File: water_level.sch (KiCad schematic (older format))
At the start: 14 parts, among them U1 LTV-847

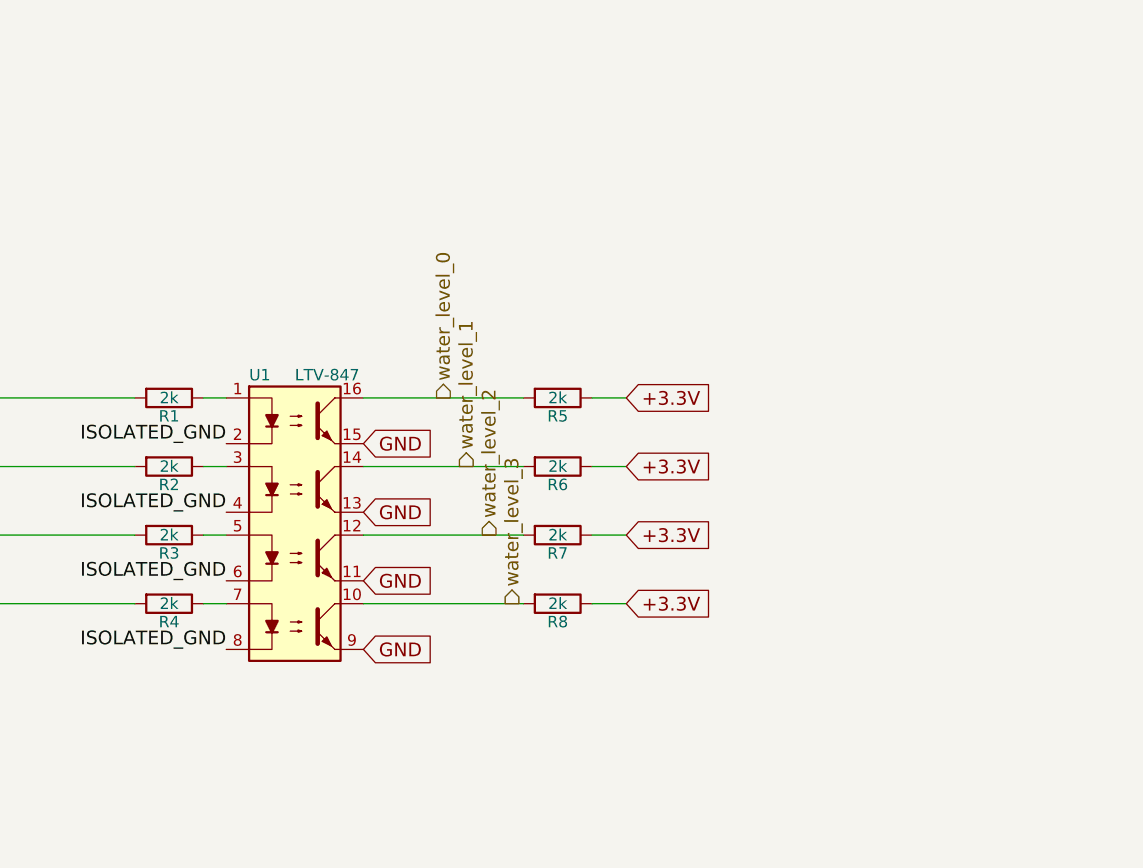
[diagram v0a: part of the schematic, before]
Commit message: fixed links to the webpage of parts
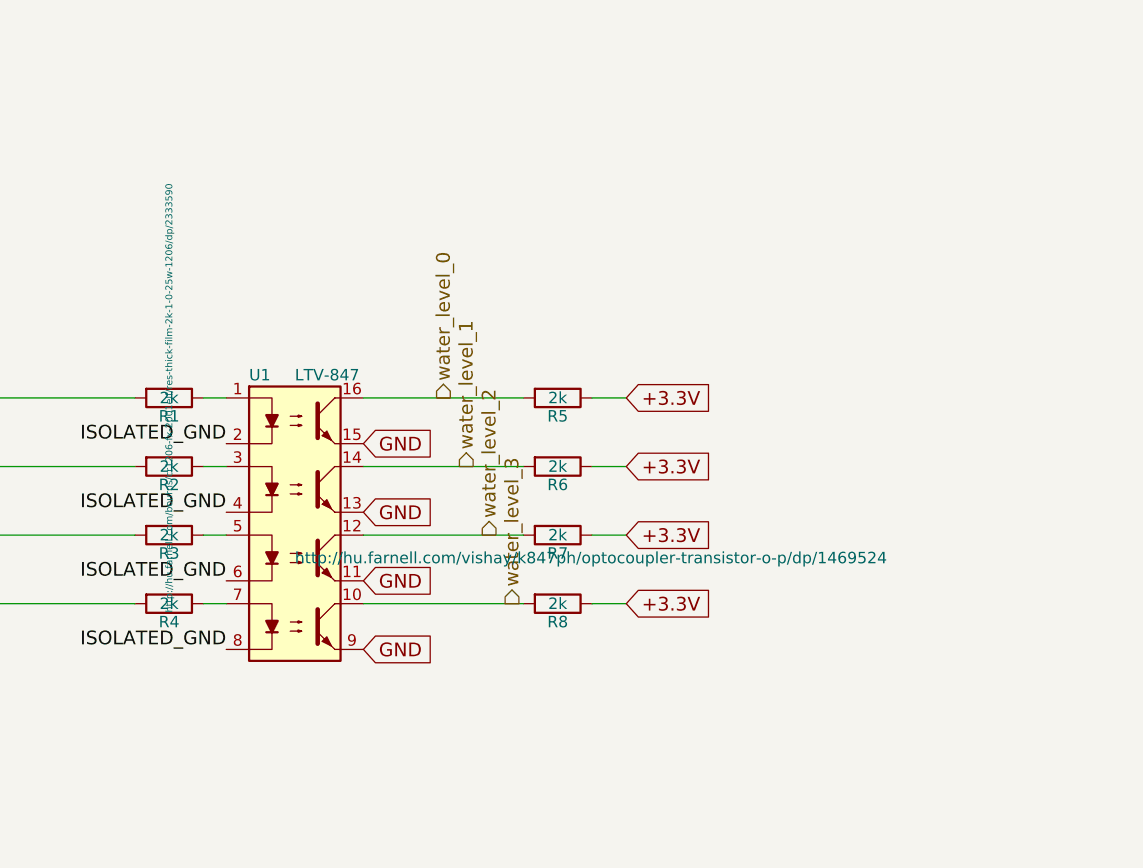
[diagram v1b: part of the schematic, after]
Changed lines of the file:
@@
 F 1 "LTV-847" H 7350 3850 50  0000 L CNN
 F 2 "Housings_SOIC:SOIC-16_3.9x9.9mm_Pitch1.27mm" H 7150 2550 50  0001 L CIN
-F 3 "" H 7350 3050 50  0000 L CNN
+F 3 "http://hu.farnell.com/vishay/k847ph/optocoupler-transistor-o-p/dp/1469524" H 7350 3050 50  0000 L CNN
 	1    7350 3150
 	1    0    0    -1
@@
 F 1 "2k" V 6800 2550 50  0000 C CNN
 F 2 "Resistors_SMD:R_1206_HandSoldering" V 6730 2550 30  0001 C CNN
-F 3 "" H 6800 2550 30  0000 C CNN
+F 3 "http://hu.farnell.com/bourns/cr1206-fx-2001elf/res-thick-film-2k-1-0-25w-1206/dp/2333590" H 6800 2550 30  0000 C CNN
 	1    6800 2550
 	0    1    1    0
@@
 F 1 "CME0303S3C" H 1500 950 60  0000 C CNN
 F 2 "water:CME0303S3C" H 1500 950 60  0001 C CNN
-F 3 "http://uk.farnell.com/murata-power-solutions/cme0303s3c/dc-dc-conv-iso-pol-1o-p-0-75w/dp/2400810" H 1500 950 60  0001 C CNN
+F 3 "http://hu.farnell.com/murata-power-solutions/cme0303s3c/dc-dc-conv-iso-pol-1o-p-0-75w/dp/2400810" H 1500 950 60  0001 C CNN
 	1    1500 950
 	1    0    0    -1

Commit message: updated links
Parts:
- DC-DC_ISOLATED1: value CME0303S3C -> MCE05S15D
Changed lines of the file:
@@
 P 1500 950
 F 0 "DC-DC_ISOLATED1" H 1550 200 60  0000 C CNN
-F 1 "CME0303S3C" H 1500 950 60  0000 C CNN
+F 1 "MCE05S15D" H 1500 950 60  0000 C CNN
 F 2 "water:CME0303S3C" H 1500 950 60  0001 C CNN
-F 3 "http://hu.farnell.com/murata-power-solutions/cme0303s3c/dc-dc-conv-iso-pol-1o-p-0-75w/dp/2400810" H 1500 950 60  0001 C CNN
+F 3 "http://hu.farnell.com/multicomp/mce05s15d/dc-dc-converter-1w-single-o-p/dp/2079693" H 1500 950 60  0001 C CNN
 	1    1500 950
 	1    0    0    -1

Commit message: stash commit before the revision of the parts
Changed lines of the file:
@@
 F 1 "LTV-847" H 7350 3850 50  0000 L CNN
 F 2 "Housings_SOIC:SOIC-16_3.9x9.9mm_Pitch1.27mm" H 7150 2550 50  0001 L CIN
-F 3 "http://hu.farnell.com/vishay/k847ph/optocoupler-transistor-o-p/dp/1469524" H 7350 3050 50  0000 L CNN
+F 3 "http://hu.farnell.com/vishay/k847ph/optocoupler-transistor-o-p/dp/1469524" H 7350 3050 50  0001 L CNN
 	1    7350 3150
 	1    0    0    -1
@@
 F 1 "2k" V 6800 2550 50  0000 C CNN
 F 2 "Resistors_SMD:R_1206_HandSoldering" V 6730 2550 30  0001 C CNN
-F 3 "http://hu.farnell.com/bourns/cr1206-fx-2001elf/res-thick-film-2k-1-0-25w-1206/dp/2333590" H 6800 2550 30  0000 C CNN
+F 3 "http://hu.farnell.com/bourns/cr1206-fx-2001elf/res-thick-film-2k-1-0-25w-1206/dp/2333590" H 6800 2550 30  0001 C CNN
 	1    6800 2550
 	0    1    1    0
@@
 +5V
 $Comp
+L Water_Level_Sensor_Connector SENS_1
+U 1 1 592601C6
+P 3600 2600
+F 0 "SENS_1" H 3450 1500 60  0000 C CNN
+F 1 "Water_Level_Sensor_Connector" H 3600 2600 60  0000 C CNN
+F 2 "Connectors_Terminal_Blocks:TerminalBlock_WAGO-804_RM5mm_5pol" H 3600 2600 60  0001 C CNN
+F 3 "http://hu.farnell.com/wago/2604-1105/tb-wire-to-brd-5pos-12awg/dp/2749668" H 3600 2600 60  0001 C CNN
+	1    3600 2600
+	1    0    0    -1
+$EndComp
+$Comp
+L Water_Level_Sensor_Connector SENS_3
+U 1 1 59260240
+P 3600 5150
+F 0 "SENS_3" H 3450 4050 60  0000 C CNN
+F 1 "Water_Level_Sensor_Connector" H 3600 5150 60  0000 C CNN
+F 2 "Connectors_Terminal_Blocks:TerminalBlock_WAGO-804_RM5mm_5pol" H 3600 5150 60  0001 C CNN
+F 3 "http://hu.farnell.com/wago/2604-1105/tb-wire-to-brd-5pos-12awg/dp/2749668" H 3600 5150 60  0001 C CNN
+	1    3600 5150
+	1    0    0    -1
+$EndComp
+$Comp
+L Water_Level_Sensor_Connector SENS_4
+U 1 1 592602C7
+P 3600 6400
+F 0 "SENS_4" H 3450 5300 60  0000 C CNN
+F 1 "Water_Level_Sensor_Connector" H 3600 6400 60  0000 C CNN
+F 2 "Connectors_Terminal_Blocks:TerminalBlock_WAGO-804_RM5mm_5pol" H 3600 6400 60  0001 C CNN
+F 3 "http://hu.farnell.com/wago/2604-1105/tb-wire-to-brd-5pos-12awg/dp/2749668" H 3600 6400 60  0001 C CNN
+	1    3600 6400
+	1    0    0    -1
+$EndComp
+Wire Wire Line
+	7650 2550 8350 2550
+Wire Wire Line
+	7650 2850 8350 2850
+Wire Wire Line
+	7650 3150 8350 3150
+Wire Wire Line
+	7650 3450 8350 3450
+Wire Wire Line
+	8800 2550 8650 2550
+Wire Wire Line
+	8800 2850 8650 2850
+Wire Wire Line
+	8800 3150 8650 3150
+Wire Wire Line
+	8800 3450 8650 3450
+Wire Wire Line
+	6950 3450 7050 3450
+Wire Wire Line
+	6950 3150 7050 3150
+Wire Wire Line
+	6950 2850 7050 2850
+Wire Wire Line
+	6950 2550 7050 2550
+Text GLabel 7650 3650 2    60   Input ~ 0
+GND
+Text GLabel 7650 3350 2    60   Input ~ 0
+GND
+Text GLabel 7650 3050 2    60   Input ~ 0
+GND
+Text GLabel 7650 2750 2    60   Input ~ 0
+GND
+Text GLabel 8800 2550 2    60   Input ~ 0
++3.3V
+Text GLabel 8800 2850 2    60   Input ~ 0
++3.3V
+Text GLabel 8800 3150 2    60   Input ~ 0
++3.3V
+Text GLabel 8800 3450 2    60   Input ~ 0
++3.3V
+Text Label 2000 1200 0    60   ~ 0
+ISOLATED_GND
+Text Label 3100 2850 2    60   ~ 0
+ISOLATED_GND
+Text Label 3100 4100 2    60   ~ 0
+ISOLATED_GND
+Text Label 3100 5400 2    60   ~ 0
+ISOLATED_GND
+Text Label 3100 6650 2    60   ~ 0
+ISOLATED_GND
+Text Label 7050 2750 2    60   ~ 0
+ISOLATED_GND
+Text Label 7050 3050 2    60   ~ 0
+ISOLATED_GND
+Text Label 7050 3350 2    60   ~ 0
+ISOLATED_GND
+Text Label 7050 3650 2    60   ~ 0
+ISOLATED_GND
+Text Label 2000 1450 0    60   ~ 0
+ISOLATED_+12V
+Text Label 3100 3000 2    60   ~ 0
+ISOLATED_+12V
+Text Label 3100 4250 2    60   ~ 0
+ISOLATED_+12V
+Text Label 3100 5550 2    60   ~ 0
+ISOLATED_+12V
+Text Label 3100 6800 2    60   ~ 0
+ISOLATED_+12V
+Text Label 3100 3150 2    60   ~ 0
+ISOLATED_+12V
+Text Label 3100 4400 2    60   ~ 0
+ISOLATED_+12V
+Text Label 3100 5700 2    60   ~ 0
+ISOLATED_+12V
+Text Label 3100 6950 2    60   ~ 0
+ISOLATED_+12V
+Wire Wire Line
+	3800 3300 4650 3300
+Wire Wire Line
+	4650 3300 4650 2550
+Wire Wire Line
+	4650 2550 6650 2550
+Wire Wire Line
+	3800 4550 4850 4550
+Wire Wire Line
+	4850 4550 4850 2850
+Wire Wire Line
+	4850 2850 6650 2850
+Wire Wire Line
+	3800 5850 5050 5850
+Wire Wire Line
+	5050 5850 5050 3150
+Wire Wire Line
+	5050 3150 6650 3150
+Wire Wire Line
+	3800 7100 5250 7100
+Wire Wire Line
+	5250 7100 5250 3450
+Wire Wire Line
+	5250 3450 6650 3450
+$Comp
 L Water_Level_Sensor_Connector SENS_2
 U 1 1 5925F963
@@
 F 1 "Water_Level_Sensor_Connector" H 3600 3850 60  0000 C CNN
 F 2 "Connectors_Terminal_Blocks:TerminalBlock_WAGO-804_RM5mm_5pol" H 3600 3850 60  0001 C CNN
-F 3 "http://hu.farnell.com/wago/2092-1375/terminal-block-wire-to-brd-5pos/dp/2352416" H 3600 3850 60  0001 C CNN
+F 3 "http://hu.farnell.com/wago/2604-1105/tb-wire-to-brd-5pos-12awg/dp/2749668" H 3600 3850 60  0001 C CNN
 	1    3600 3850
 	1    0    0    -1
 $EndComp
-$Comp
-L Water_Level_Sensor_Connector SENS_1
-U 1 1 592601C6
-P 3600 2600
-F 0 "SENS_1" H 3450 1500 60  0000 C CNN
-F 1 "Water_Level_Sensor_Connector" H 3600 2600 60  0000 C CNN
-F 2 "Connectors_Terminal_Blocks:TerminalBlock_WAGO-804_RM5mm_5pol" H 3600 2600 60  0001 C CNN
-F 3 "http://hu.farnell.com/wago/2092-1375/terminal-block-wire-to-brd-5pos/dp/2352416" H 3600 2600 60  0001 C CNN
-	1    3600 2600
-	1    0    0    -1
-$EndComp
-$Comp
-L Water_Level_Sensor_Connector SENS_3
-U 1 1 59260240
-P 3600 5150
-F 0 "SENS_3" H 3450 4050 60  0000 C CNN
-F 1 "Water_Level_Sensor_Connector" H 3600 5150 60  0000 C CNN
-F 2 "Connectors_Terminal_Blocks:TerminalBlock_WAGO-804_RM5mm_5pol" H 3600 5150 60  0001 C CNN
-F 3 "http://hu.farnell.com/wago/2092-1375/terminal-block-wire-to-brd-5pos/dp/2352416" H 3600 5150 60  0001 C CNN
-	1    3600 5150
-	1    0    0    -1
-$EndComp
-$Comp
-L Water_Level_Sensor_Connector SENS_4
-U 1 1 592602C7
-P 3600 6400
-F 0 "SENS_4" H 3450 5300 60  0000 C CNN
-F 1 "Water_Level_Sensor_Connector" H 3600 6400 60  0000 C CNN
-F 2 "Connectors_Terminal_Blocks:TerminalBlock_WAGO-804_RM5mm_5pol" H 3600 6400 60  0001 C CNN
-F 3 "http://hu.farnell.com/wago/2092-1375/terminal-block-wire-to-brd-5pos/dp/2352416" H 3600 6400 60  0001 C CNN
-	1    3600 6400
-	1    0    0    -1
-$EndComp
-Wire Wire Line
-	7650 2550 8350 2550
-Wire Wire Line
-	7650 2850 8350 2850
-Wire Wire Line
-	7650 3150 8350 3150
-Wire Wire Line
-	7650 3450 8350 3450
-Wire Wire Line
-	8800 2550 8650 2550
-Wire Wire Line
-	8800 2850 8650 2850
-Wire Wire Line
-	8800 3150 8650 3150
-Wire Wire Line
-	8800 3450 8650 3450
-Wire Wire Line
-	6950 3450 7050 3450
-Wire Wire Line
-	6950 3150 7050 3150
-Wire Wire Line
-	6950 2850 7050 2850
-Wire Wire Line
-	6950 2550 7050 2550
-Text GLabel 7650 3650 2    60   Input ~ 0
-GND
-Text GLabel 7650 3350 2    60   Input ~ 0
-GND
-Text GLabel 7650 3050 2    60   Input ~ 0
-GND
-Text GLabel 7650 2750 2    60   Input ~ 0
-GND
-Text GLabel 8800 2550 2    60   Input ~ 0
-+3.3V
-Text GLabel 8800 2850 2    60   Input ~ 0
-+3.3V
-Text GLabel 8800 3150 2    60   Input ~ 0
-+3.3V
-Text GLabel 8800 3450 2    60   Input ~ 0
-+3.3V
-Text Label 2000 1200 0    60   ~ 0
-ISOLATED_GND
-Text Label 3100 2850 2    60   ~ 0
-ISOLATED_GND
-Text Label 3100 4100 2    60   ~ 0
-ISOLATED_GND
-Text Label 3100 5400 2    60   ~ 0
-ISOLATED_GND
-Text Label 3100 6650 2    60   ~ 0
-ISOLATED_GND
-Text Label 7050 2750 2    60   ~ 0
-ISOLATED_GND
-Text Label 7050 3050 2    60   ~ 0
-ISOLATED_GND
-Text Label 7050 3350 2    60   ~ 0
-ISOLATED_GND
-Text Label 7050 3650 2    60   ~ 0
-ISOLATED_GND
-Text Label 2000 1450 0    60   ~ 0
-ISOLATED_+12V
-Text Label 3100 3000 2    60   ~ 0
-ISOLATED_+12V
-Text Label 3100 4250 2    60   ~ 0
-ISOLATED_+12V
-Text Label 3100 5550 2    60   ~ 0
-ISOLATED_+12V
-Text Label 3100 6800 2    60   ~ 0
-ISOLATED_+12V
-Text Label 3100 3150 2    60   ~ 0
-ISOLATED_+12V
-Text Label 3100 4400 2    60   ~ 0
-ISOLATED_+12V
-Text Label 3100 5700 2    60   ~ 0
-ISOLATED_+12V
-Text Label 3100 6950 2    60   ~ 0
-ISOLATED_+12V
-Wire Wire Line
-	3800 3300 4650 3300
-Wire Wire Line
-	4650 3300 4650 2550
-Wire Wire Line
-	4650 2550 6650 2550
-Wire Wire Line
-	3800 4550 4850 4550
-Wire Wire Line
-	4850 4550 4850 2850
-Wire Wire Line
-	4850 2850 6650 2850
-Wire Wire Line
-	3800 5850 5050 5850
-Wire Wire Line
-	5050 5850 5050 3150
-Wire Wire Line
-	5050 3150 6650 3150
-Wire Wire Line
-	3800 7100 5250 7100
-Wire Wire Line
-	5250 7100 5250 3450
-Wire Wire Line
-	5250 3450 6650 3450
 $EndSCHEMATC

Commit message: parts corrected after review; dc/dc converter has to be ordered
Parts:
- DC-DC_ISOLATED1: footprint water:CME0303S3C -> water:MCE05S15D
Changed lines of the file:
@@
 F 0 "DC-DC_ISOLATED1" H 1550 200 60  0000 C CNN
 F 1 "MCE05S15D" H 1500 950 60  0000 C CNN
-F 2 "water:CME0303S3C" H 1500 950 60  0001 C CNN
+F 2 "water:MCE05S15D" H 1500 950 60  0001 C CNN
 F 3 "http://hu.farnell.com/multicomp/mce05s15d/dc-dc-converter-1w-single-o-p/dp/2079693" H 1500 950 60  0001 C CNN
 	1    1500 950

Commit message: before wiring
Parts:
- renumbered U1 to U2
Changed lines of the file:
@@
 $EndDescr
 $Comp
-L LTV-847 U1
+L LTV-847 U2
 U 1 1 56150C6A
 P 7350 3150
-F 0 "U1" H 7150 3850 50  0000 L CNN
+F 0 "U2" H 7150 3850 50  0000 L CNN
 F 1 "LTV-847" H 7350 3850 50  0000 L CNN
 F 2 "Housings_SOIC:SOIC-16_3.9x9.9mm_Pitch1.27mm" H 7150 2550 50  0001 L CIN

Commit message: shields corrected; wago connectors connected
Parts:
- SENS_1, SENS_2, SENS_3, SENS_4: footprint Connectors_Terminal_Blocks:TerminalBlock_WAGO-804_RM5mm_5pol -> water:5x2_TerminalBlock_WAGO-2604-1105
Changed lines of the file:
@@
 F 0 "SENS_1" H 3450 1500 60  0000 C CNN
 F 1 "Water_Level_Sensor_Connector" H 3600 2600 60  0000 C CNN
-F 2 "Connectors_Terminal_Blocks:TerminalBlock_WAGO-804_RM5mm_5pol" H 3600 2600 60  0001 C CNN
+F 2 "water:5x2_TerminalBlock_WAGO-2604-1105" H 3600 2600 60  0001 C CNN
 F 3 "http://hu.farnell.com/wago/2604-1105/tb-wire-to-brd-5pos-12awg/dp/2749668" H 3600 2600 60  0001 C CNN
 	1    3600 2600
@@
 F 0 "SENS_3" H 3450 4050 60  0000 C CNN
 F 1 "Water_Level_Sensor_Connector" H 3600 5150 60  0000 C CNN
-F 2 "Connectors_Terminal_Blocks:TerminalBlock_WAGO-804_RM5mm_5pol" H 3600 5150 60  0001 C CNN
+F 2 "water:5x2_TerminalBlock_WAGO-2604-1105" H 3600 5150 60  0001 C CNN
 F 3 "http://hu.farnell.com/wago/2604-1105/tb-wire-to-brd-5pos-12awg/dp/2749668" H 3600 5150 60  0001 C CNN
 	1    3600 5150
@@
 F 0 "SENS_4" H 3450 5300 60  0000 C CNN
 F 1 "Water_Level_Sensor_Connector" H 3600 6400 60  0000 C CNN
-F 2 "Connectors_Terminal_Blocks:TerminalBlock_WAGO-804_RM5mm_5pol" H 3600 6400 60  0001 C CNN
+F 2 "water:5x2_TerminalBlock_WAGO-2604-1105" H 3600 6400 60  0001 C CNN
 F 3 "http://hu.farnell.com/wago/2604-1105/tb-wire-to-brd-5pos-12awg/dp/2749668" H 3600 6400 60  0001 C CNN
 	1    3600 6400
@@
 F 0 "SENS_2" H 3450 2750 60  0000 C CNN
 F 1 "Water_Level_Sensor_Connector" H 3600 3850 60  0000 C CNN
-F 2 "Connectors_Terminal_Blocks:TerminalBlock_WAGO-804_RM5mm_5pol" H 3600 3850 60  0001 C CNN
+F 2 "water:5x2_TerminalBlock_WAGO-2604-1105" H 3600 3850 60  0001 C CNN
 F 3 "http://hu.farnell.com/wago/2604-1105/tb-wire-to-brd-5pos-12awg/dp/2749668" H 3600 3850 60  0001 C CNN
 	1    3600 3850
